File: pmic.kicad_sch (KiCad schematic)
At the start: 63 parts, among them J401 EMI shield frame, U401 STPMIC1DPQR

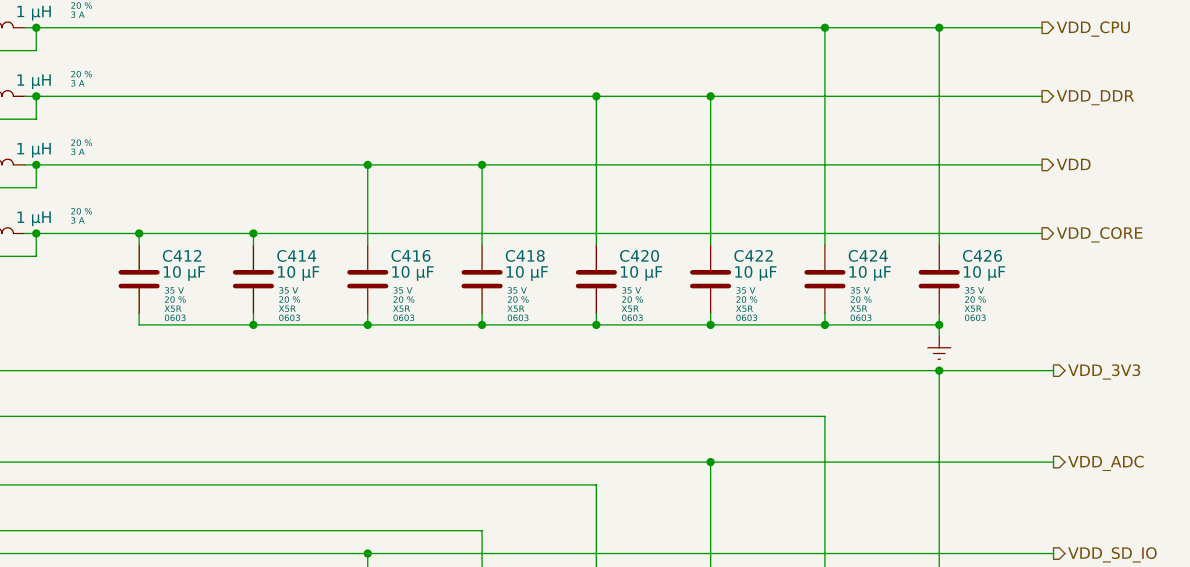
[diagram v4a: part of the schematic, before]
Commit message: Fix symbols and footprint assignments
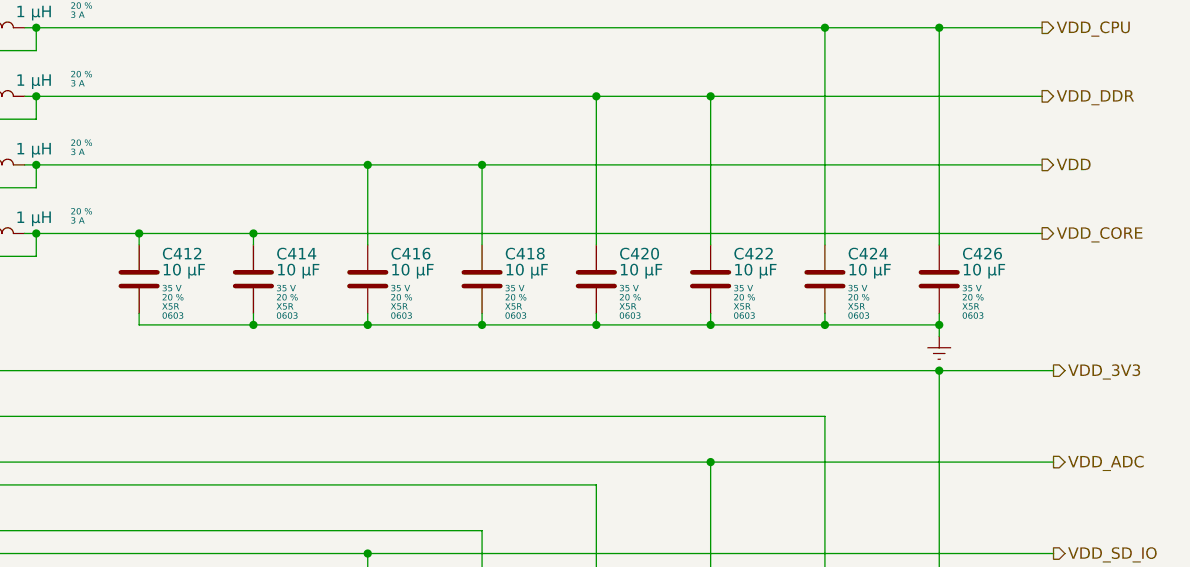
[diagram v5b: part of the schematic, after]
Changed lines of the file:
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@@
 		(dnp no)
 		(property "Reference" "C420"
-			(at 281.94 139.7 0)
+			(at 281.94 139.446 0)
 			(effects
 				(font
@@
 		)
 		(property "Value" "10 µF"
-			(at 281.94 141.478 0)
+			(at 281.94 141.224 0)
 			(effects
 				(font
@@
 		)
 		(property "Voltage rating" "35 V"
-			(at 282.194 143.51 0)
+			(at 281.94 143.256 0)
 			(effects
 				(font
@@
 		)
 		(property "Tolerance" "20 %"
-			(at 282.194 144.526 0)
+			(at 281.94 144.272 0)
 			(effects
 				(font
@@
 		)
 		(property "Temperature coefficient" "X5R"
-			(at 282.194 145.542 0)
+			(at 281.94 145.288 0)
 			(effects
 				(font
@@
 		)
 		(property "Size" "0603"
-			(at 282.194 146.558 0)
+			(at 281.94 146.304 0)
 			(effects
 				(font
@@
 		(dnp no)
 		(property "Reference" "C422"
-			(at 294.64 139.7 0)
+			(at 294.64 139.446 0)
 			(effects
 				(font
@@
 		)
 		(property "Value" "10 µF"
-			(at 294.64 141.478 0)
+			(at 294.64 141.224 0)
 			(effects
 				(font
@@
 		)
 		(property "Voltage rating" "35 V"
-			(at 294.894 143.51 0)
+			(at 294.64 143.256 0)
 			(effects
 				(font
@@
 		)
 		(property "Tolerance" "20 %"
-			(at 294.894 144.526 0)
+			(at 294.64 144.272 0)
 			(effects
 				(font
@@
 		)
 		(property "Temperature coefficient" "X5R"
-			(at 294.894 145.542 0)
+			(at 294.64 145.288 0)
 			(effects
 				(font
@@
 		)
 		(property "Size" "0603"
-			(at 294.894 146.558 0)
+			(at 294.64 146.304 0)
 			(effects
 				(font
@@
 		(dnp no)
 		(property "Reference" "C426"
-			(at 320.04 139.7 0)
+			(at 320.04 139.446 0)
 			(effects
 				(font
@@
 		)
 		(property "Value" "10 µF"
-			(at 320.04 141.478 0)
+			(at 320.04 141.224 0)
 			(effects
 				(font
@@
 		)
 		(property "Voltage rating" "35 V"
-			(at 320.294 143.51 0)
+			(at 320.04 143.256 0)
 			(effects
 				(font
@@
 		)
 		(property "Tolerance" "20 %"
-			(at 320.294 144.526 0)
+			(at 320.04 144.272 0)
 			(effects
 				(font
@@
 		)
 		(property "Temperature coefficient" "X5R"
-			(at 320.294 145.542 0)
+			(at 320.04 145.288 0)
 			(effects
 				(font
@@
 		)
 		(property "Size" "0603"
-			(at 320.294 146.558 0)
+			(at 320.04 146.304 0)
 			(effects
 				(font
@@
 		(dnp no)
 		(property "Reference" "C418"
-			(at 269.24 139.7 0)
+			(at 269.24 139.446 0)
 			(effects
 				(font
@@
 		)
 		(property "Value" "10 µF"
-			(at 269.24 141.478 0)
+			(at 269.24 141.224 0)
 			(effects
 				(font
@@
 		)
 		(property "Voltage rating" "35 V"
-			(at 269.494 143.51 0)
+			(at 269.24 143.256 0)
 			(effects
 				(font
@@
 		)
 		(property "Tolerance" "20 %"
-			(at 269.494 144.526 0)
+			(at 269.24 144.272 0)
 			(effects
 				(font
@@
 		)
 		(property "Temperature coefficient" "X5R"
-			(at 269.494 145.542 0)
+			(at 269.24 145.288 0)
 			(effects
 				(font
@@
 		)
 		(property "Size" "0603"
-			(at 269.494 146.558 0)
+			(at 269.24 146.304 0)
 			(effects
 				(font
@@
 		(dnp no)
 		(property "Reference" "C412"
-			(at 231.14 139.7 0)
+			(at 231.14 139.446 0)
 			(effects
 				(font
@@
 		)
 		(property "Value" "10 µF"
-			(at 231.14 141.478 0)
+			(at 231.14 141.224 0)
 			(effects
 				(font
@@
 		)
 		(property "Voltage rating" "35 V"
-			(at 231.394 143.51 0)
+			(at 231.14 143.256 0)
 			(effects
 				(font
@@
 		)
 		(property "Tolerance" "20 %"
-			(at 231.394 144.526 0)
+			(at 231.14 144.272 0)
 			(effects
 				(font
@@
 		)
 		(property "Temperature coefficient" "X5R"
-			(at 231.394 145.542 0)
+			(at 231.14 145.288 0)
 			(effects
 				(font
@@
 		)
 		(property "Size" "0603"
-			(at 231.394 146.558 0)
+			(at 231.14 146.304 0)
 			(effects
 				(font
@@
 		(dnp no)
 		(property "Reference" "C414"
-			(at 243.84 139.7 0)
+			(at 243.84 139.446 0)
 			(effects
 				(font
@@
 		)
 		(property "Value" "10 µF"
-			(at 243.84 141.478 0)
+			(at 243.84 141.224 0)
 			(effects
 				(font
@@
 		)
 		(property "Voltage rating" "35 V"
-			(at 244.094 143.51 0)
+			(at 243.84 143.256 0)
 			(effects
 				(font
@@
 		)
 		(property "Tolerance" "20 %"
-			(at 244.094 144.526 0)
+			(at 243.84 144.272 0)
 			(effects
 				(font
@@
 		)
 		(property "Temperature coefficient" "X5R"
-			(at 244.094 145.542 0)
+			(at 243.84 145.288 0)
 			(effects
 				(font
@@
 		)
 		(property "Size" "0603"
-			(at 244.094 146.558 0)
+			(at 243.84 146.304 0)
 			(effects
 				(font
@@
 	)
 	(symbol
-		(lib_name "R_1")
+		(lib_name "R_2")
 		(lib_id "Device:R")
 		(at 134.62 193.04 90)
@@
 		(dnp no)
 		(property "Reference" "C424"
-			(at 307.34 139.7 0)
+			(at 307.34 139.446 0)
 			(effects
 				(font
@@
 		)
 		(property "Value" "10 µF"
-			(at 307.34 141.478 0)
+			(at 307.34 141.224 0)
 			(effects
 				(font
@@
 		)
 		(property "Voltage rating" "35 V"
-			(at 307.594 143.51 0)
+			(at 307.34 143.256 0)
 			(effects
 				(font
@@
 		)
 		(property "Tolerance" "20 %"
-			(at 307.594 144.526 0)
+			(at 307.34 144.272 0)
 			(effects
 				(font
@@
 		)
 		(property "Temperature coefficient" "X5R"
-			(at 307.594 145.542 0)
+			(at 307.34 145.288 0)
 			(effects
 				(font
@@
 		)
 		(property "Size" "0603"
-			(at 307.594 146.558 0)
+			(at 307.34 146.304 0)
 			(effects
 				(font
@@
 		(dnp no)
 		(property "Reference" "C416"
-			(at 256.54 139.7 0)
+			(at 256.54 139.446 0)
 			(effects
 				(font
@@
 		)
 		(property "Value" "10 µF"
-			(at 256.54 141.478 0)
+			(at 256.54 141.224 0)
 			(effects
 				(font
@@
 		)
 		(property "Voltage rating" "35 V"
-			(at 256.794 143.51 0)
+			(at 256.54 143.256 0)
 			(effects
 				(font
@@
 		)
 		(property "Tolerance" "20 %"
-			(at 256.794 144.526 0)
+			(at 256.54 144.272 0)
 			(effects
 				(font
@@
 		)
 		(property "Temperature coefficient" "X5R"
-			(at 256.794 145.542 0)
+			(at 256.54 145.288 0)
 			(effects
 				(font
@@
 		)
 		(property "Size" "0603"
-			(at 256.794 146.558 0)
+			(at 256.54 146.304 0)
 			(effects
 				(font

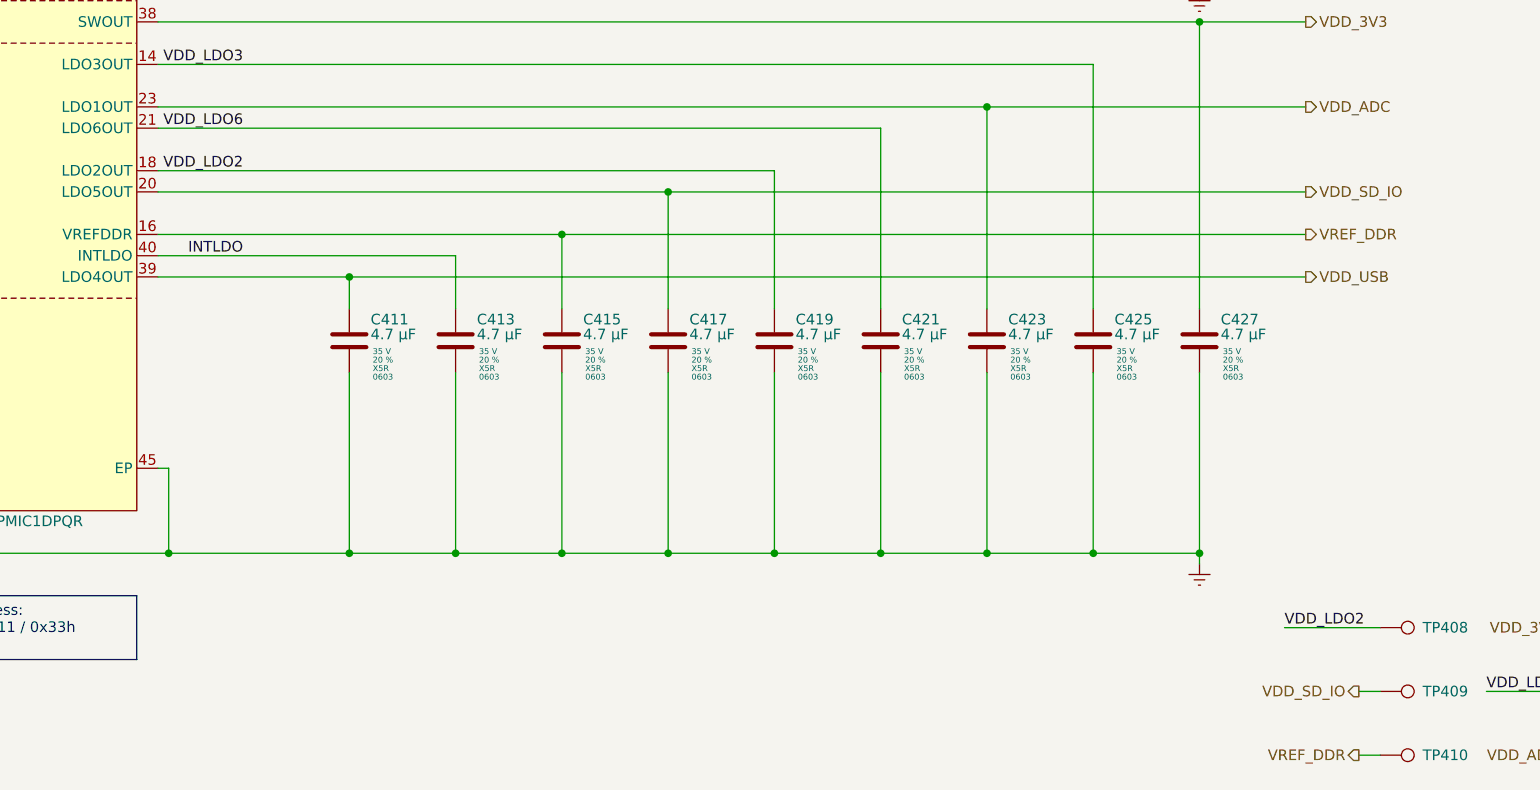
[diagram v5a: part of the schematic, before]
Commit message: Refactor SD card interface
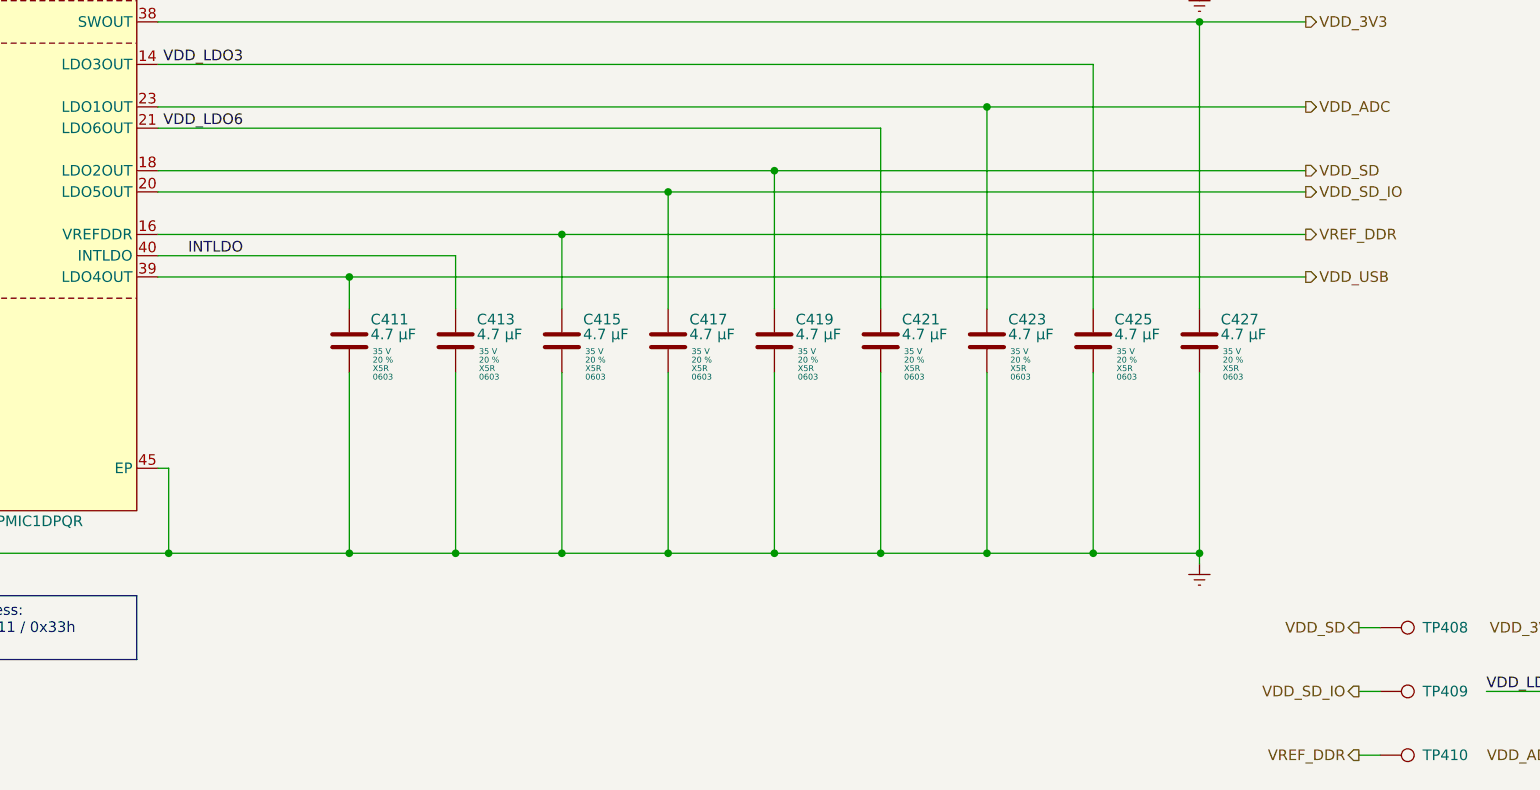
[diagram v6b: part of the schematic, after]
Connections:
- net VDD_LDO2 renamed VDD_SD
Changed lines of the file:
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@@
+	)
+	(junction
+		(at 266.7 170.18)
+		(diameter 0)
+		(color 0 0 0 0)
 	)
 	(junction
@@
 	(wire
 		(pts
-			(xy 327.66 224.79) (xy 339.09 224.79)
+			(xy 336.55 224.79) (xy 339.09 224.79)
 		)
 		(stroke
@@
 		(pts
 			(xy 121.92 176.53) (xy 134.62 176.53)
+		)
+		(stroke
+			(width 0)
+			(type default)
+		)
+	)
+	(wire
+		(pts
+			(xy 266.7 170.18) (xy 330.2 170.18)
 		)
 		(stroke
@@
 		)
 	)
-	(label "VDD_LDO2"
-		(at 203.2 170.18 180)
-		(effects
-			(font
-				(size 1.27 1.27)
-			)
-			(justify right bottom)
-		)
-	)
 	(label "VDD_LDO6"
 		(at 351.79 247.65 0)
@@
 			)
 			(justify right bottom)
-		)
-	)
-	(label "VDD_LDO2"
-		(at 327.66 224.79 0)
-		(effects
-			(font
-				(size 1.27 1.27)
-			)
-			(justify left bottom)
 		)
 	)
@@
 		)
 	)
+	(hierarchical_label "VDD_SD"
+		(shape output)
+		(at 336.55 224.79 180)
+		(effects
+			(font
+				(size 1.27 1.27)
+			)
+			(justify right)
+		)
+	)
 	(hierarchical_label "VDD_DDR"
 		(shape output)
@@
 		)
 	)
+	(hierarchical_label "VDD_SD"
+		(shape output)
+		(at 330.2 170.18 0)
+		(effects
+			(font
+				(size 1.27 1.27)
+			)
+			(justify left)
+		)
+	)

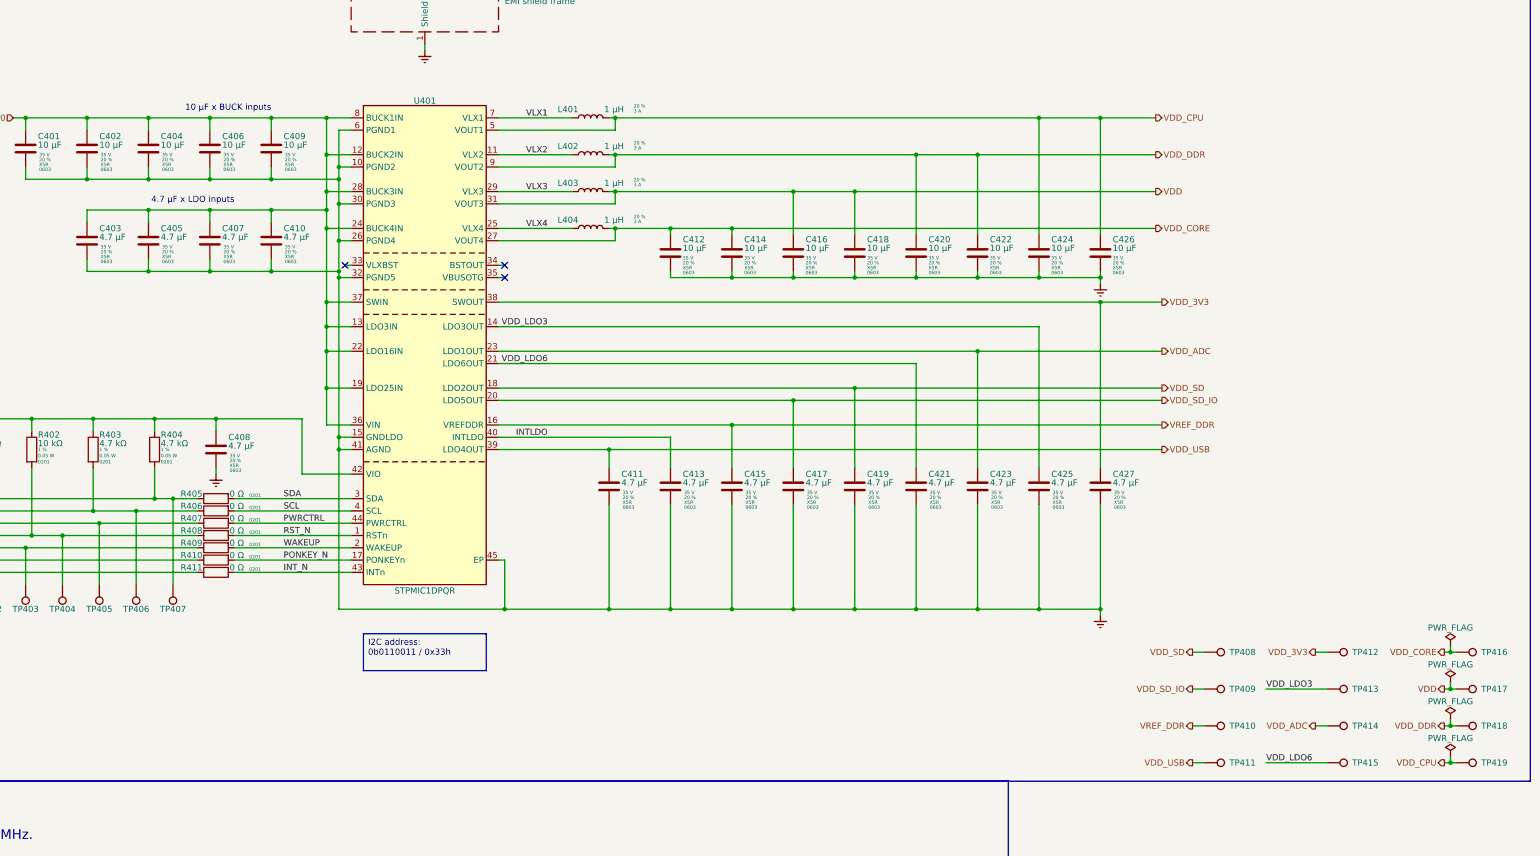
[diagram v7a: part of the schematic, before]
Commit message: Fix power connections
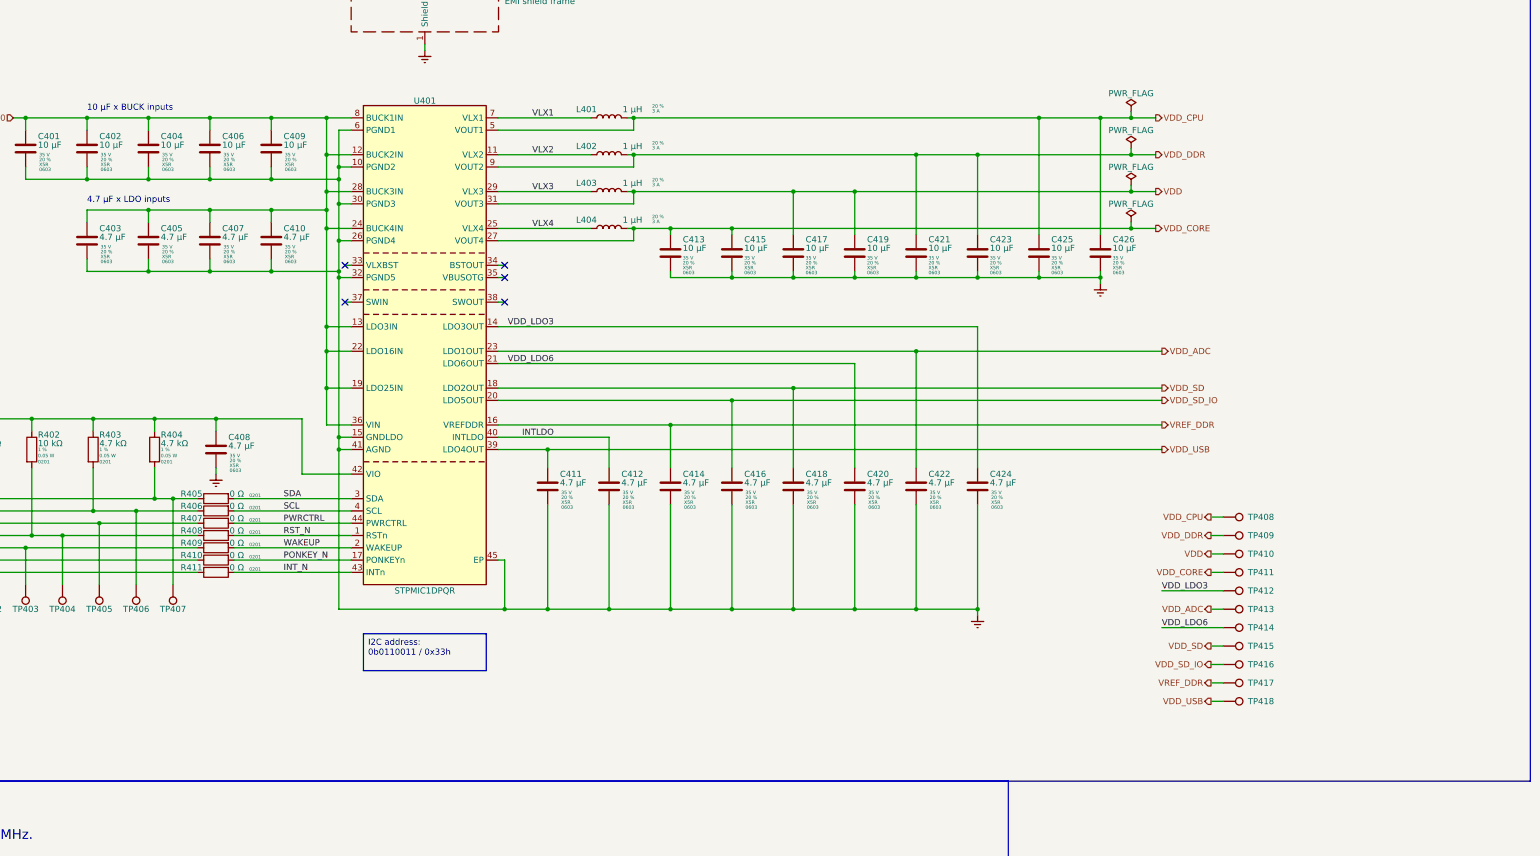
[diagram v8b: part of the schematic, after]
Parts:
- removed C427: 4.7 µF, Capacitor_SMD:C_0603_1608Metric, symbol Device:C
- removed TP412: TestPoint, TestPoint:TestPoint_Pad_D1.0mm, symbol Connector:TestPoint
- renumbered C413 to C412, C412 to C413, C415 to C414, C414 to C415, C417 to C416, C416 to C417, C419 to C418, C418 to C419, C421 to C420, C420 to C421, C423 to C422, C422 to C423, C425 to C424, C424 to C425, TP419 to TP408, TP418 to TP409, TP417 to TP410, TP416 to TP411, TP413 to TP412, TP414 to TP413, TP415 to TP414, TP408 to TP415, TP409 to TP416, TP410 to TP417, TP411 to TP418
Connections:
- net V_5V0: no longer U401.37 (SWIN)
- net VDD_3V3: no longer names the net of U401.38 (SWOUT)
- no-connect marks 3 -> 5
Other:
- moved on the sheet: C411, C412, C414, C416, C418, C420, C422, C424, L401, L402, L403, L404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
